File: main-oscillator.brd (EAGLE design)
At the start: 100 x 30.5 mm, 15 parts, among them IC1 7805TV, IC2 UA555N

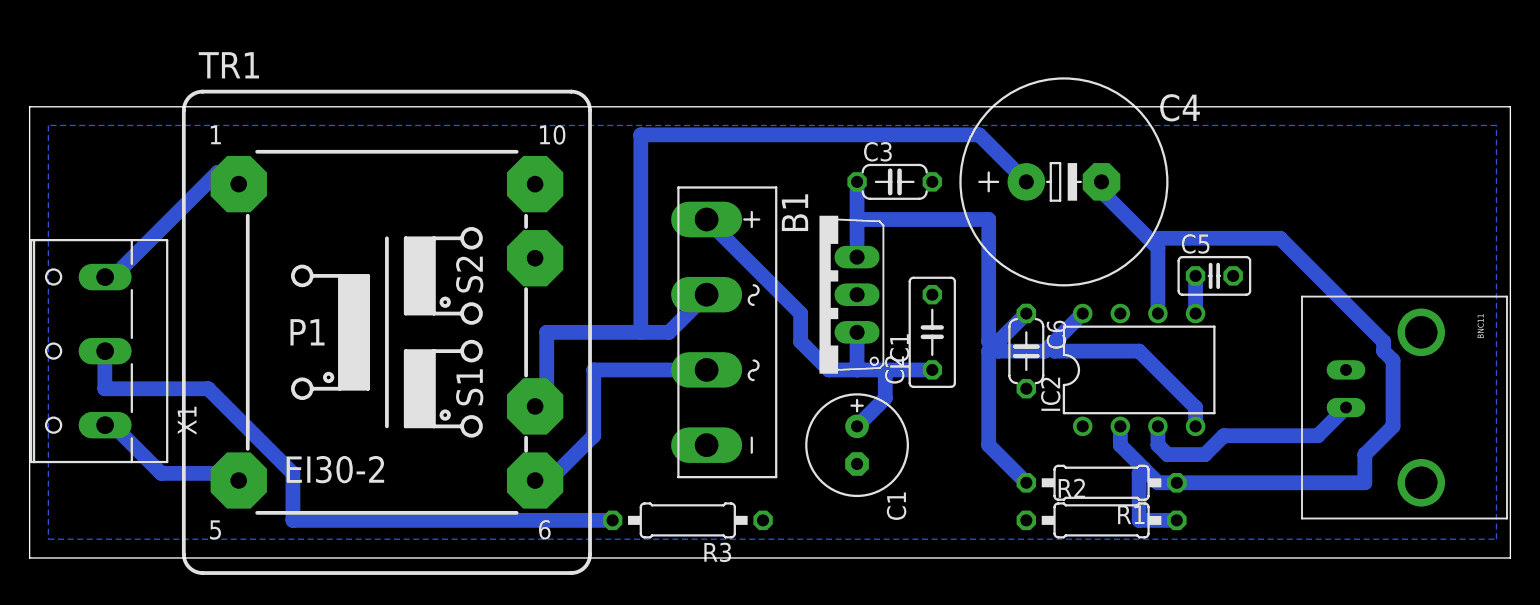
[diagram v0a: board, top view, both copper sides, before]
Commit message: Smaller transformer, DIL package for rectifier bridge. More compact design.
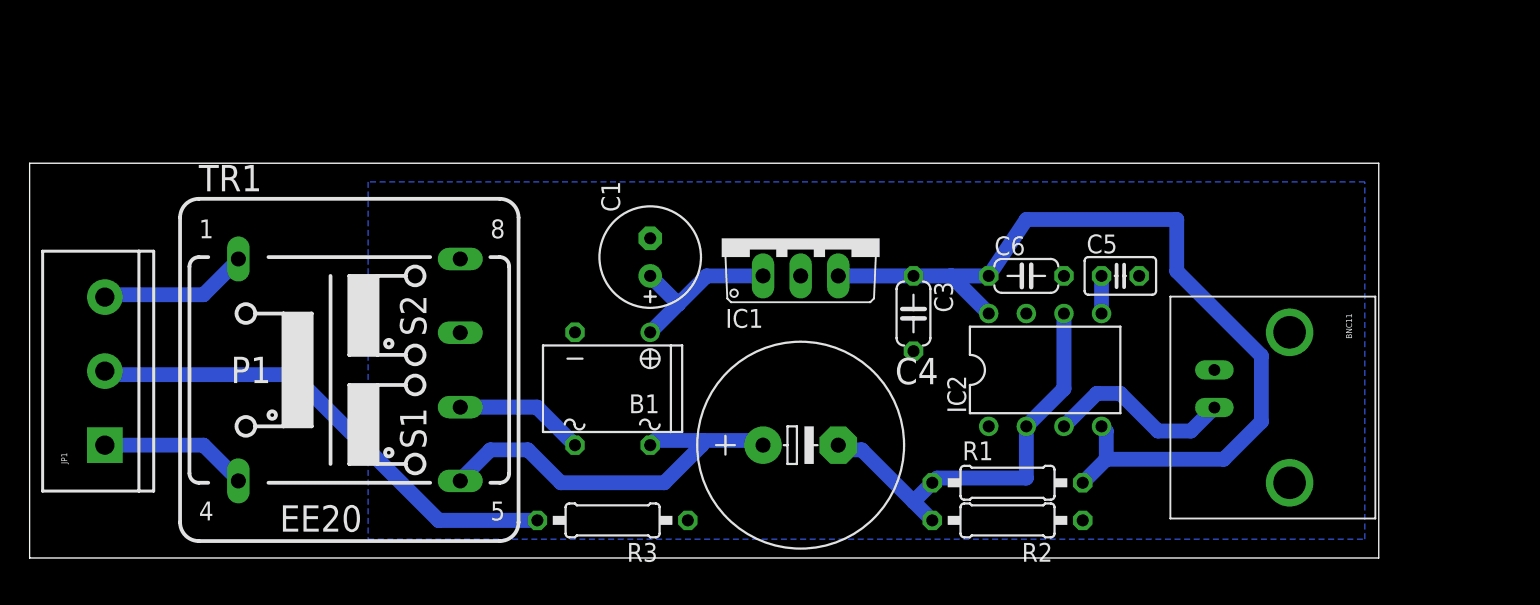
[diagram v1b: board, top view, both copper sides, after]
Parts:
- removed C2: 470n, rcl:C050-030X075
- removed X1: (no value), con-wago-500:W237-103
- added JP1: mains, SparkFun-Connectors:SCREWTERMINAL-5MM-3
- B1: device rectifier:KBL -> rectifier:B-DIL
- R1: value 1k -> 100R
- R3: value 330k -> 220k
- TR1: value 230-9V -> 230-6V; device trafo:EI30-2 -> trafo:EE20-2
- moved C4 25.1 mm to (52.1, 7.62)
- moved C1 18.9 mm to (41.9, 20.3), turned to 90 degrees
- moved C3 8.98 mm to (59.7, 16.5), turned to 270 degrees
- moved BNC11 8.89 mm to (80.0, 10.2)
- moved B1 8.52 mm to (39.4, 11.4), turned to 180 degrees
- moved C5 6.35 mm to (73.7, 19.1)
- moved IC2 6.35 mm to (68.6, 12.7)
- moved R1 6.35 mm to (66.0, 5.08), turned to 0 degrees
- moved R2 6.35 mm to (66.0, 2.54), turned to 180 degrees
- moved R3 5.08 mm to (39.4, 2.54)
- moved C6 5.08 mm to (67.3, 19.1), turned to 0 degrees
- moved IC1 4.02 mm to (52.1, 21.6), turned to 0 degrees
- moved TR1 3.59 mm to (21.6, 12.7)
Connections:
- net GND: no longer C2.2
- net N$1: now also JP1.3; no longer X1.3
- net N$2: now also TR1.5; no longer TR1.7
- net N$3: now also JP1.1, TR1.4; no longer TR1.5, X1.1
- net N$4: now also JP1.2; no longer X1.2
- net N$5: no longer C2.1
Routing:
- net N$8: track 64.6 -> 28.9 mm
- net N$2: track 58.0 -> 27.4 mm
- net N$5: track 27.7 -> 11.9 mm
- net N$4: track 42.4 -> 33.5 mm
- net N$6: track 17.4 -> 8.81 mm
- net V+: track 56.2 -> 60.6 mm
- net N$9: track 15.5 -> 12.8 mm
- net N$1: track 12.6 -> 10.2 mm
- net N$3: track 10.7 -> 10.0 mm
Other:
- board size 100 x 30.5 mm -> 91.1 x 26.7 mm

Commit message: Compact design.
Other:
- board size 91.1 x 26.7 mm -> 89.8 x 26.7 mm
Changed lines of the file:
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@@
 <board>
 <plain>
-<wire x1="0" y1="0" x2="91.11" y2="0" width="0" layer="20"/>
-<wire x1="91.11" y1="0" x2="91.11" y2="26.66" width="0" layer="20"/>
-<wire x1="91.11" y1="26.66" x2="0" y2="26.66" width="0" layer="20"/>
+<wire x1="0" y1="0" x2="89.84" y2="0" width="0" layer="20"/>
+<wire x1="89.84" y1="0" x2="89.84" y2="26.66" width="0" layer="20"/>
+<wire x1="89.84" y1="26.66" x2="0" y2="26.66" width="0" layer="20"/>
 <wire x1="0" y1="26.66" x2="0" y2="0" width="0" layer="20"/>
 <dimension x1="0" y1="25.39" x2="0" y2="0" x3="-3.81" y3="12.695" textsize="1.778" layer="20"/>
-<dimension x1="0" y1="0" x2="91.11" y2="0" x3="45.555" y3="-5.08" textsize="1.778" layer="20"/>
+<dimension x1="0" y1="0" x2="89.84" y2="0" x3="44.92" y3="-5.08" textsize="1.778" layer="20"/>
 </plain>
 <attributes>
@@
 <vertex x="22.86" y="25.4"/>
 <vertex x="22.86" y="1.27"/>
-<vertex x="90.17" y="1.27"/>
-<vertex x="90.17" y="25.4"/>
+<vertex x="88.9" y="1.27"/>
+<vertex x="88.9" y="25.4"/>
 </polygon>
 </signal>

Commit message: v 1.1: added switch gitignore updated with 'stuff' folder
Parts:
- added S1: (no value), switch:320-916
- moved C1 10.2 mm to (52.1, 20.3)
- moved IC1 10.2 mm to (62.2, 21.6)
- moved C5 5.08 mm to (78.7, 19.1)
- moved C6 5.08 mm to (72.4, 19.1)
- moved IC2 5.08 mm to (73.7, 12.7)
- moved JP1 4.02 mm to (6.35, 3.81)
- moved R1 4.02 mm to (69.8, 6.35)
- moved R2 4.02 mm to (69.8, 3.81)
- moved B1 3.81 mm to (43.2, 11.4), turned to 0 degrees
- moved C4 3.81 mm to (55.9, 7.62)
- moved R3 3.81 mm to (43.2, 2.54)
- moved TR1 3.81 mm to (25.4, 12.7)
- moved BNC11 3.81 mm to (83.8, 10.2)
- moved C3 2.84 mm to (62.2, 15.2), turned to 180 degrees
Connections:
- new net N$10: JP1.3, S1.3
- net N$1: now also S1.2; no longer JP1.3
- net N$2: now also TR1.7; no longer TR1.5
- net N$6: now also TR1.8; no longer TR1.6
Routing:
- net N$5: track 11.9 -> 23.8 mm
- net N$10: track 0.00 -> 7.58 mm
- net N$2: track 27.4 -> 33.9 mm
- net N$6: track 8.81 -> 14.9 mm
- net N$1: track 10.2 -> 13.7 mm
- net N$3: track 10.0 -> 12.4 mm
- net V+: track 60.6 -> 59.2 mm
- net N$9: track 12.8 -> 11.8 mm
- net N$4: track 33.5 -> 34.3 mm
- net N$8: track 28.9 -> 28.2 mm
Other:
- board size 89.8 x 26.7 mm -> 93.7 x 31.7 mm
